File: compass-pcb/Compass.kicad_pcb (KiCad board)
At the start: 2 copper layers, 10 parts

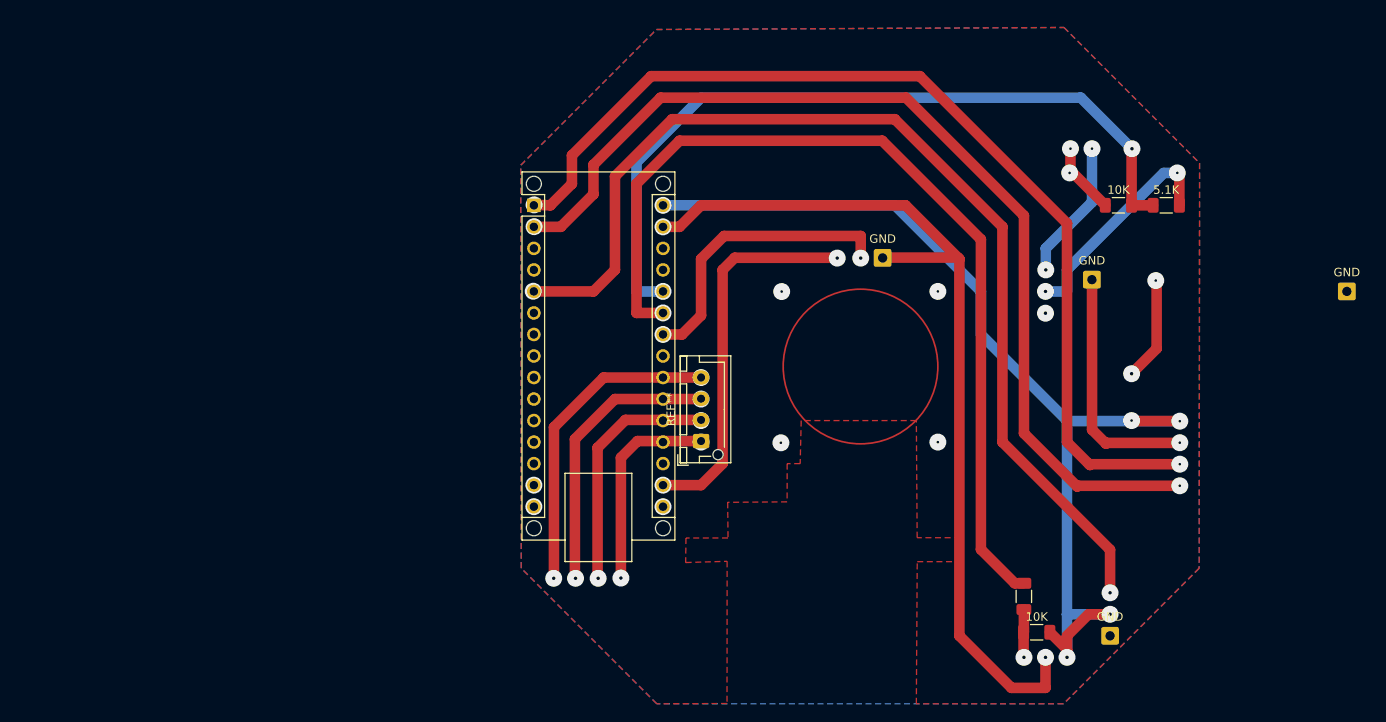
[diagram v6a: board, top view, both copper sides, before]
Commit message: adding alignment anchors
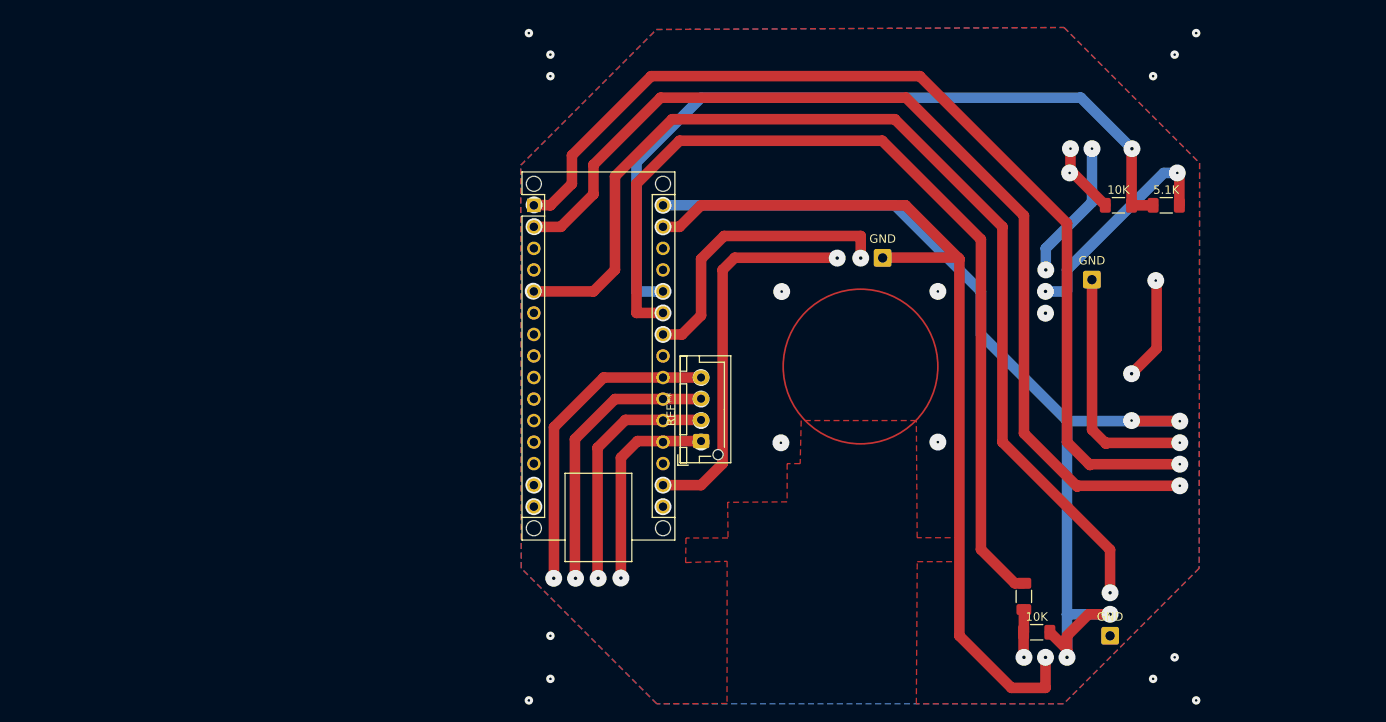
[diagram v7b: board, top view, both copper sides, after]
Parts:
- removed the GND at (264.2, 86.4)
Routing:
- net (no net): vias 41 -> 53
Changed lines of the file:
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@@
-    )
-  )
-  (footprint "Connector_Wire:SolderWire-0.5sqmm_1x01_D0.9mm_OD2.1mm" (layer "F.Cu")
-    (at 264.16 86.36)
-    (descr "Soldered wire connection, for a single 0.5 mm² wire, basic insulation, conductor diameter 0.9mm, outer diameter 2.1mm, size source Multi-Contact FLEXI-E 0.5 (https://ec.staubli.com/AcroFiles/Catalogues/TM_Cab-Main-11014119_(en)_hi.pdf), bend radius 3 times outer diameter, generated with kicad-footprint-generator")
-    (tags "connector wire 0.5sqmm")
-    (attr exclude_from_pos_files exclude_from_bom)
-    (fp_text reference "GND" (at 0 -2.25) (layer "F.SilkS")
-        (effects (font (size 1 1) (thickness 0.15)))
-    )
-    (fp_text value " " (at 0 2.25) (layer "F.Fab") hide
-        (effects (font (size 1 1) (thickness 0.15)))
-    )
-    (fp_text user "${REFERENCE}" (at 0 0) (layer "F.Fab") hide
-        (effects (font (size 0.52 0.52) (thickness 0.08)))
-    )
-    (fp_line (start -1.8 -1.55) (end -1.8 1.55)
-      (stroke (width 0.05) (type solid)) (layer "F.CrtYd"))
-    (fp_line (start -1.8 1.55) (end 1.8 1.55)
-      (stroke (width 0.05) (type solid)) (layer "F.CrtYd"))
-    (fp_line (start 1.8 -1.55) (end -1.8 -1.55)
-      (stroke (width 0.05) (type solid)) (layer "F.CrtYd"))
-    (fp_line (start 1.8 1.55) (end 1.8 -1.55)
-      (stroke (width 0.05) (type solid)) (layer "F.CrtYd"))
-    (fp_circle (center 0 0) (end 1.05 0)
-      (stroke (width 0.1) (type solid)) (fill none) (layer "F.Fab"))
-    (pad "" thru_hole roundrect (at 0 0) (size 2.1 2.1) (drill 1.1) (layers "*.Cu" "*.Mask") (roundrect_rratio 0.119048)
-      (net 1 "GND"))
-    (pad "" thru_hole roundrect (at 0 0) (size 2.1 2.1) (drill 1.1) (layers "*.Cu" "*.Mask") (roundrect_rratio 0.119048)
-      (net 1 "GND"))
-    (model "${KICAD6_3DMODEL_DIR}/Connector_Wire.3dshapes/SolderWire-0.5sqmm_1x01_D0.9mm_OD2.1mm.wrl"
-      (offset (xyz 0 0 0))
-      (scale (xyz 1 1 1))
-      (rotate (xyz 0 0 0))
     )
   )
@@
   (via (at 178.497355 120.181435) (size 2) (drill 0.4) (layers "F.Cu" "B.Cu") (free) (net 0))
   (via (at 175.81554 120.211112) (size 2) (drill 0.4) (layers "F.Cu" "B.Cu") (net 0))
+  (via (at 167.64 134.62) (size 1) (drill 0.3) (layers "F.Cu" "B.Cu") (net 0))
   (via (at 168.154242 86.338073) (size 2) (drill 0.4) (layers "F.Cu" "B.Cu") (net 0))
+  (via (at 170.18 127) (size 1) (drill 0.3) (layers "F.Cu" "B.Cu") (net 0))
   (via (at 197.470447 86.37722) (size 2) (drill 0.3) (layers "F.Cu" "B.Cu") (net 0))
   (via (at 183.467723 86.36) (size 2) (drill 0.4) (layers "F.Cu" "B.Cu") (net 0))
   (via (at 226.06 129.54) (size 2) (drill 0.4) (layers "F.Cu" "B.Cu") (net 0))
+  (via (at 241.3 132.08) (size 1) (drill 0.3) (layers "F.Cu" "B.Cu") (net 0))
   (via (at 183.467723 109.22) (size 2) (drill 0.4) (layers "F.Cu" "B.Cu") (net 0))
   (via (at 183.467723 91.44) (size 2) (drill 0.4) (layers "F.Cu" "B.Cu") (net 0))
   (via (at 241.610913 85.077314) (size 2) (drill 0.3) (layers "F.Cu" "B.Cu") (net 0))
   (via (at 168.227723 111.76) (size 2) (drill 0.3) (layers "F.Cu" "B.Cu") (net 0))
+  (via (at 170.18 132.08) (size 1) (drill 0.3) (layers "F.Cu" "B.Cu") (net 0))
+  (via (at 246.38 134.62) (size 1) (drill 0.3) (layers "F.Cu" "B.Cu") (net 0))
   (via (at 168.227723 109.22) (size 2) (drill 0.3) (layers "F.Cu" "B.Cu") (net 0))
   (via (at 244.447756 106.747484) (size 2) (drill 0.3) (layers "F.Cu" "B.Cu") (net 0))
   (via (at 228.635081 83.82) (size 2) (drill 0.4) (layers "F.Cu" "B.Cu") (net 0))
   (via (at 183.467723 76.2) (size 2) (drill 0.4) (layers "F.Cu" "B.Cu") (net 0))
+  (via (at 243.84 129.54) (size 1) (drill 0.3) (layers "F.Cu" "B.Cu") (net 0))
   (via (at 204.025111 82.428689) (size 2) (drill 0.4) (layers "F.Cu" "B.Cu") (net 0))
   (via (at 183.467723 111.76) (size 2) (drill 0.3) (layers "F.Cu" "B.Cu") (net 0))
@@
   (via (at 197.380327 104.221065) (size 2) (drill 0.3) (layers "F.Cu" "B.Cu") (net 0))
   (via (at 170.570809 120.211112) (size 2) (drill 0.4) (layers "F.Cu" "B.Cu") (net 0))
+  (via (at 241.3 60.96) (size 1) (drill 0.3) (layers "F.Cu" "B.Cu") (net 0))
   (via (at 236.22 121.92) (size 2) (drill 0.4) (layers "F.Cu" "B.Cu") (net 0))
+  (via (at 170.18 58.42) (size 1) (drill 0.3) (layers "F.Cu" "B.Cu") (net 0))
   (via (at 228.6 88.932887) (size 2) (drill 0.4) (layers "F.Cu" "B.Cu") (net 0))
   (via (at 228.6 86.36) (size 2) (drill 0.4) (layers "F.Cu" "B.Cu") (free) (net 0))
@@
   (via (at 215.9 104.14) (size 2) (drill 0.3) (layers "F.Cu" "B.Cu") (net 0))
   (via (at 187.96 104.14) (size 2) (drill 0.3) (layers "F.Cu" "B.Cu") (net 0))
+  (via (at 246.38 55.88) (size 1) (drill 0.3) (layers "F.Cu" "B.Cu") (net 0))
+  (via (at 243.84 58.42) (size 1) (drill 0.3) (layers "F.Cu" "B.Cu") (net 0))
   (via (at 238.76 96.069029) (size 2) (drill 0.4) (layers "F.Cu" "B.Cu") (net 0))
   (via (at 187.96 101.595) (size 2) (drill 0.3) (layers "F.Cu" "B.Cu") (net 0))
+  (via (at 167.64 55.88) (size 1) (drill 0.3) (layers "F.Cu" "B.Cu") (net 0))
   (via (at 244.447756 109.292484) (size 2) (drill 0.3) (layers "F.Cu" "B.Cu") (net 0))
   (via (at 215.9 86.36) (size 2) (drill 0.3) (layers "F.Cu" "B.Cu") (net 0))
   (via (at 187.96 96.52) (size 2) (drill 0.3) (layers "F.Cu" "B.Cu") (net 0))
   (via (at 231.450913 72.377314) (size 2) (drill 0.3) (layers "F.Cu" "B.Cu") (net 0))
+  (via (at 170.18 60.96) (size 1) (drill 0.3) (layers "F.Cu" "B.Cu") (net 0))
   (segment (start 180.34 86.36) (end 183.467723 86.36) (width 1.25) (layer "B.Cu") (net 0))
   (segment (start 234.087449 75.827632) (end 228.635081 81.28) (width 1.25) (layer "B.Cu") (net 0))

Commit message: comments for anchors
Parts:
- moved 10K 59.5 mm to (168.1, 125.3)
- moved 10K 59.5 mm to (177.8, 75.0)
- moved 5.1K 59.5 mm to (166.6, 121.1)
- moved 5.1K 59.5 mm to (183.4, 75.0)
- moved GND 59.5 mm to (174.6, 83.7)
- moved GND 59.5 mm to (149.9, 81.2)
- moved GND 59.5 mm to (176.8, 125.8)
- moved REF** 59.5 mm to (128.5, 102.8)
- moved REF** 59.5 mm to (108.8, 75.0)
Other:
- board text added: "Alignment anchors: 1) print stencil 2) drill these holes 3) align back side stencil by these holes"
